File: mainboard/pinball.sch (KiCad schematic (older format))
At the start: 32 parts, among them CON1 AVR-ISP-6, IC1 ATMEGA328-A, J1 Conn_01x14, J2 Conn_01x02, J3 Conn_01x03_Male, P1 SCREW_PLACEHOLDER, P2 SCREW_PLACEHOLDER, P3 SCREW_PLACEHOLDER, P4 SCREW_PLACEHOLDER, P5 PWR, P7 CONN_02X24, Q1 Q_NMOS_GDS, Q3 Q_NMOS_GDS, Q5 Q_NMOS_GDS, Q7 Q_NMOS_GDS, U1 R-78B5.0-2.0, U2 Teensy3.2, U3 74AHC125, Y1 Crystal

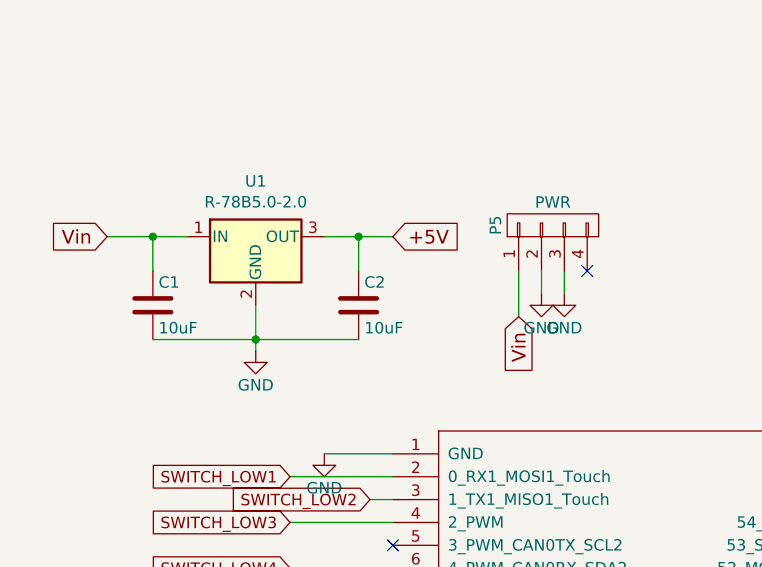
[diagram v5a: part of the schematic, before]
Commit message: Remove 5V regulator. Power directly from MOLEX connector instead. Add CC-BY-SA license.
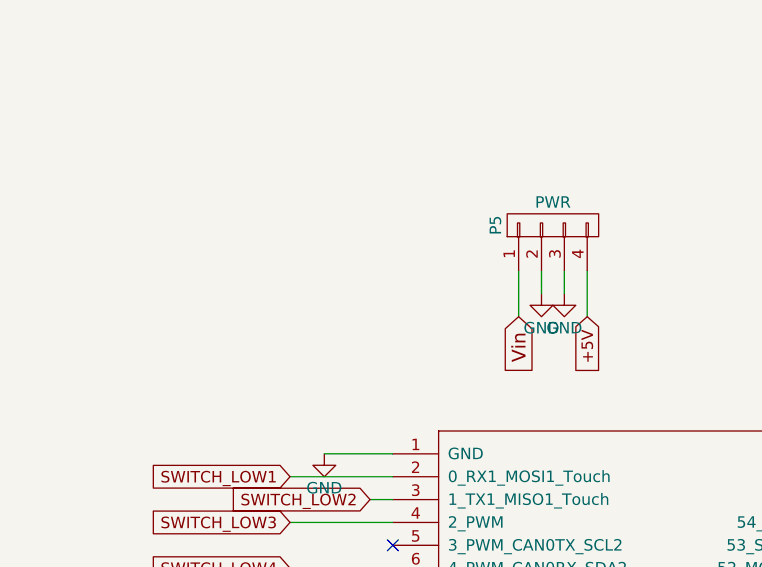
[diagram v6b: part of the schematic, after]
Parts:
- removed C1, C2: 10uF, Capacitors_SMD:C_0603, symbol pinball-rescue:C
- removed U1: R-78B5.0-2.0, Power_Integrations:TO-220, symbol Regulator_Linear:L7805
- P5: Digikey # (none) -> A25422-ND
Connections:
- net +5V: now also P5.4 (P4)
- no-connect marks 66 -> 65
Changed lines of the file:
@@
 Text GLabel 4350 5100 2    60   Input ~ 0
 +5V
-$Comp
-L pinball-rescue:C C1
-U 1 1 5AC53D1A
-P 1150 1150
-F 0 "C1" H 1175 1250 50  0000 L CNN
-F 1 "10uF" H 1175 1050 50  0000 L CNN
-F 2 "Capacitors_SMD:C_0603" H 1188 1000 50  0001 C CNN
-F 3 "" H 1150 1150 50  0001 C CNN
-F 4 "490-3298-1-ND" H 1150 1150 60  0001 C CNN "Digikey #"
-	1    1150 1150
-	1    0    0    -1
-$EndComp
-$Comp
-L pinball-rescue:C C2
-U 1 1 5AC53E32
-P 2050 1150
-F 0 "C2" H 2075 1250 50  0000 L CNN
-F 1 "10uF" H 2075 1050 50  0000 L CNN
-F 2 "Capacitors_SMD:C_0603" H 2088 1000 50  0001 C CNN
-F 3 "" H 2050 1150 50  0001 C CNN
-F 4 "490-3298-1-ND" H 2050 1150 60  0001 C CNN "Digikey #"
-	1    2050 1150
-	1    0    0    -1
-$EndComp
-$Comp
-L power:GND #PWR02
-U 1 1 5AC53E69
-P 1600 1350
-F 0 "#PWR02" H 1600 1100 50  0001 C CNN
-F 1 "GND" H 1600 1200 50  0000 C CNN
-F 2 "" H 1600 1350 50  0001 C CNN
-F 3 "" H 1600 1350 50  0001 C CNN
-	1    1600 1350
-	1    0    0    -1
-$EndComp
-Text GLabel 2200 850  2    60   Input ~ 0
-+5V
-Text GLabel 950  850  0    60   Input ~ 0
-Vin
 Text GLabel 4350 5900 2    60   Input ~ 0
 SDA
@@
 F 2 "Terminal_Blocks:TerminalBlock_Pheonix_MKDS1.5-4pol" H 2900 800 50  0001 C CNN
 F 3 "" H 2900 800 50  0000 C CNN
+F 4 "A25422-ND " H 2900 800 50  0001 C CNN "Digikey #"
 	1    2900 800
 	0    -1   -1   0
@@
 	1    0    0    -1
 $EndComp
-NoConn ~ 3050 1000
 Wire Wire Line
 	2750 1000 2750 1200
@@
 Text GLabel 6350 5650 1    50   Input ~ 0
 SCORE_OUT4A
-Wire Wire Line
-	950  850  1150 850
-Wire Wire Line
-	1150 1000 1150 850
-Connection ~ 1150 850
-Wire Wire Line
-	2050 1000 2050 850
-Connection ~ 2050 850
-Wire Wire Line
-	2050 850  2200 850
-Wire Wire Line
-	2050 1300 1600 1300
-Wire Wire Line
-	1600 1150 1600 1300
-Connection ~ 1600 1300
-Wire Wire Line
-	1600 1300 1150 1300
-Wire Wire Line
-	1600 1300 1600 1350
 Text GLabel 1700 3900 0    50   Input ~ 0
 SWITCH_LOW16
@@
 NoConn ~ 4200 5400
 NoConn ~ 2200 3200
-$Comp
-L Regulator_Linear:L7805 U1
-U 1 1 5C8325C2
-P 1600 850
-F 0 "U1" H 1600 1092 50  0000 C CNN
-F 1 "R-78B5.0-2.0" H 1600 1001 50  0000 C CNN
-F 2 "Power_Integrations:TO-220" H 1625 700 50  0001 L CIN
-F 3 "http://www.st.com/content/ccc/resource/technical/document/datasheet/41/4f/b3/b0/12/d4/47/88/CD00000444.pdf/files/CD00000444.pdf/jcr:content/translations/en.CD00000444.pdf" H 1600 800 50  0001 C CNN
-F 4 "945-3042-ND" H 1600 850 50  0001 C CNN "Digikey #"
-	1    1600 850
-	1    0    0    -1
-$EndComp
-Wire Wire Line
-	1900 850  2050 850
-Wire Wire Line
-	1150 850  1300 850
 NoConn ~ 4200 5700
 Wire Wire Line
@@
 	2200 2700 1750 2700
 NoConn ~ 2200 2200
+Text GLabel 3050 1200 3    50   Input ~ 0
++5V
+Wire Wire Line
+	3050 1000 3050 1200
 $EndSCHEMATC
